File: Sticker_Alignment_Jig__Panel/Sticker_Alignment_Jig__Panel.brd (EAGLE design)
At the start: 200 x 100 mm, 13 parts

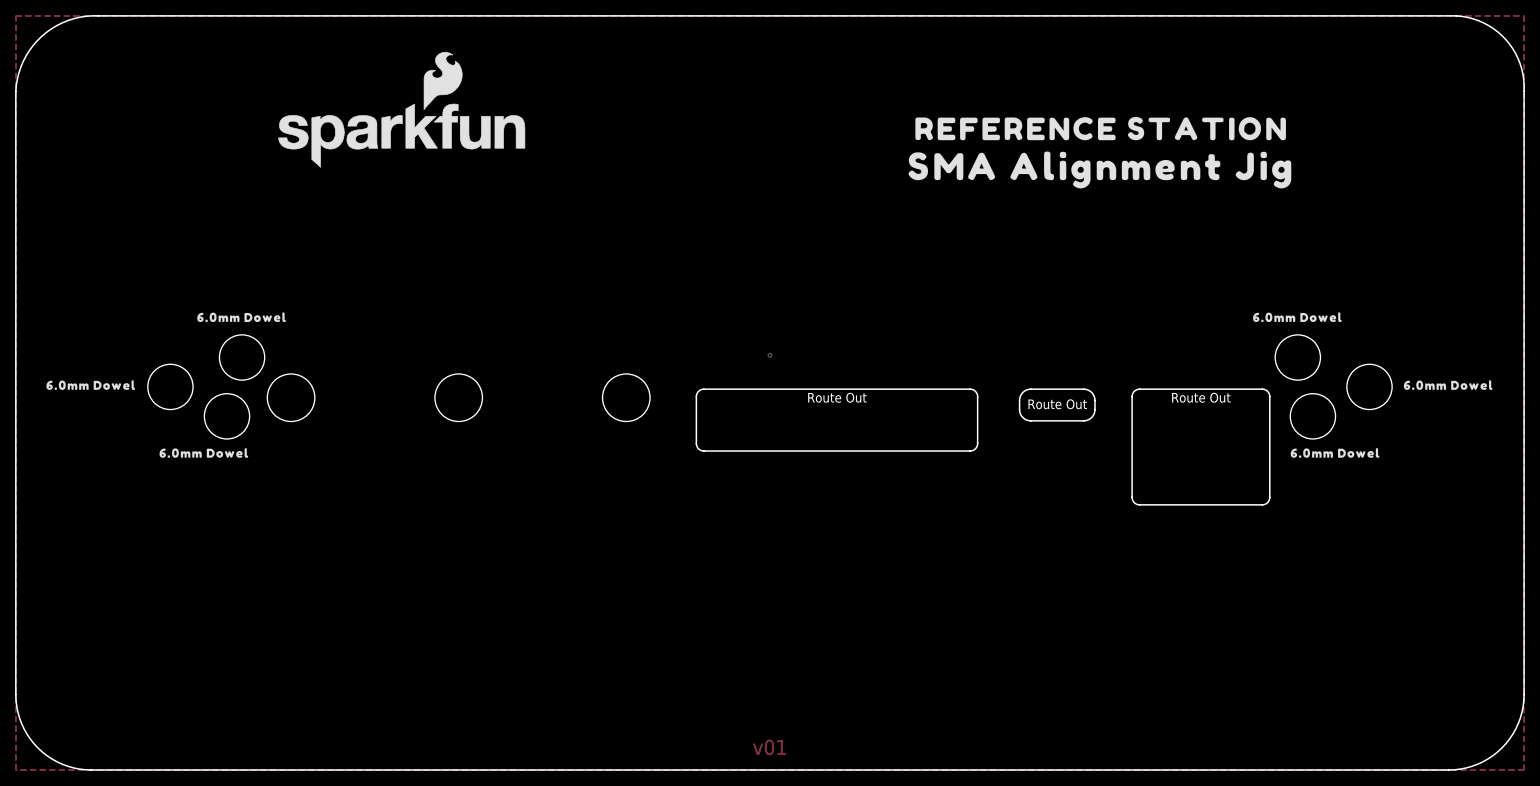
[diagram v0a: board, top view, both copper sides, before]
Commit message: Update sticker alignment jig
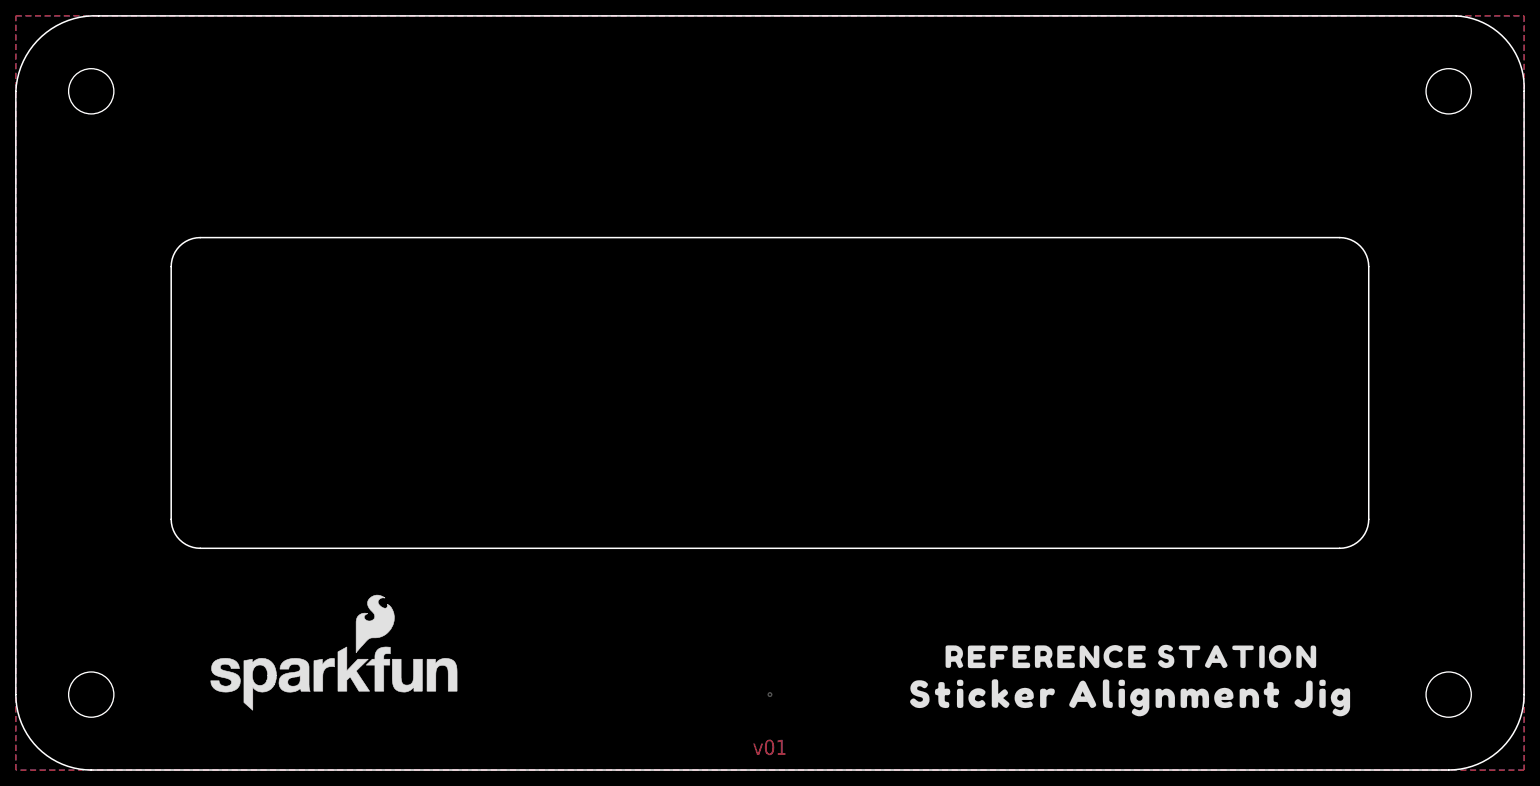
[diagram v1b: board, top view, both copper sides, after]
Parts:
- removed U$10, U$11, U$6, U$7, U$8, U$9: (no value), output:6#0MM_DOWEL0
- removed U$2: 3.5MM_CONNECTOR, CORS_Panels:3.5MM_CONNECTOR
- removed U$3: USB-C, CORS_Panels:USB-C
- removed U$4: ETHERNET, CORS_Panels:ETHERNET
- U$5: device output:SMA_ALIGNMENT_JIG0 -> output:STICKER_ALIGNMENT_JIG0
- moved LOGO1 72.6 mm to (-57.9, -37.9)
- moved U$1 70.1 mm to (48.0, -35.0)
- moved U$5 70.1 mm to (48.0, -40.0)
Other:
- outline, holes or cut-outs redrawn
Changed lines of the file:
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@@
 <drawing>
 <settings>
-<setting alwaysvectorfont="yes"/>
+<setting alwaysvectorfont="no"/>
 <setting verticaltext="up"/>
 </settings>
@@
 <wire x1="-100" y1="40" x2="-100" y2="-40" width="0.2" layer="20"/>
 <text x="0" y="-48" size="2" layer="1" font="vector" ratio="15" align="bottom-center">v01</text>
-<wire x1="76.2" y1="0" x2="-76.2" y2="0" width="0.2" layer="51"/>
-<wire x1="76.2" y1="1.6" x2="-76.2" y2="1.6" width="0.2" layer="51"/>
-<wire x1="-76.2" y1="0" x2="-76.2" y2="1.6" width="0.2" layer="51"/>
-<wire x1="76.2" y1="0" x2="76.2" y2="1.6" width="0.2" layer="51"/>
-<hole x="-79.5" y="0.8" drill="6"/>
-<hole x="79.5" y="0.8" drill="6"/>
-<hole x="-72" y="-3.1" drill="6"/>
-<hole x="-19.05" y="-0.635" drill="6.3"/>
-<hole x="-41.275" y="-0.635" drill="6.3"/>
-<hole x="-63.5" y="-0.635" drill="6.3"/>
-<hole x="-70" y="4.7" drill="6"/>
-<hole x="70" y="4.7" drill="6"/>
-<hole x="72" y="-3.1" drill="6"/>
+<wire x1="-79.4" y1="16.75" x2="-79.4" y2="-16.75" width="0.2" layer="20"/>
+<wire x1="-75.55" y1="-20.6" x2="75.55" y2="-20.6" width="0.2" layer="20"/>
+<wire x1="79.4" y1="-16.75" x2="79.4" y2="16.75" width="0.2" layer="20"/>
+<wire x1="75.55" y1="20.6" x2="-75.55" y2="20.6" width="0.2" layer="20"/>
+<wire x1="-75.55" y1="-20.6" x2="-79.4" y2="-16.75" width="0.2" layer="20" curve="-90"/>
+<hole x="-90" y="40" drill="6"/>
+<hole x="90" y="40" drill="6"/>
+<hole x="90" y="-40" drill="6"/>
+<hole x="-90" y="-40" drill="6"/>
+<wire x1="79.4" y1="-16.75" x2="75.55" y2="-20.6" width="0.2" layer="20" curve="-90"/>
+<wire x1="75.55" y1="20.6" x2="79.4" y2="16.75" width="0.2" layer="20" curve="-90"/>
+<wire x1="-79.4" y1="16.75" x2="-75.55" y2="20.6" width="0.2" layer="20" curve="-90"/>
 </plain>
 <attributes>
@@
 </autorouter>
 <elements>
-<element name="LOGO1" library="SparkFun-Aesthetics" package="SFE_LOGO_NAME_FLAME_.3" value="SFE_LOGO_NAME_FLAME.3_INCH" x="-48.8504" y="34.0889" smashed="yes"/>
-<element name="U$1" library="output" package="REFERENCE_STATION0" value="" x="44" y="35" smashed="yes"/>
+<element name="LOGO1" library="SparkFun-Aesthetics" package="SFE_LOGO_NAME_FLAME_.3" value="SFE_LOGO_NAME_FLAME.3_INCH" x="-57.8504" y="-37.9111" smashed="yes"/>
+<element name="U$1" library="output" package="REFERENCE_STATION0" value="" x="48" y="-35" smashed="yes"/>
 <element name="FRAME1" library="SparkFun-Aesthetics" package="CREATIVE_COMMONS" value="FRAME-LETTER" x="-25" y="-59" smashed="yes">
 <attribute name="DESIGNER" value="" x="-25" y="-59" size="1.778" layer="27" ratio="15" display="off"/>
 <attribute name="REV" value="" x="-25" y="-59" size="1.778" layer="27" ratio="15" display="off"/>
 </element>
-<element name="U$2" library="CORS_Panels" package="3.5MM_CONNECTOR" value="3.5MM_CONNECTOR" x="8.89" y="0" smashed="yes" rot="R180"/>
-<element name="U$3" library="CORS_Panels" package="USB-C" value="USB-C" x="38.1" y="0" smashed="yes" rot="R180"/>
-<element name="U$4" library="CORS_Panels" package="ETHERNET" value="ETHERNET" x="57.15" y="0" smashed="yes" rot="R180"/>
-<element name="U$5" library="output" package="SMA_ALIGNMENT_JIG0" value="" x="44" y="30" smashed="yes"/>
-<element name="U$6" library="output" package="6#0MM_DOWEL0" value="" x="70" y="10" smashed="yes"/>
-<element name="U$7" library="output" package="6#0MM_DOWEL0" value="" x="90" y="1" smashed="yes"/>
-<element name="U$8" library="output" package="6#0MM_DOWEL0" value="" x="75" y="-8" smashed="yes"/>
-<element name="U$9" library="output" package="6#0MM_DOWEL0" value="" x="-75" y="-8" smashed="yes"/>
-<element name="U$10" library="output" package="6#0MM_DOWEL0" value="" x="-90" y="1" smashed="yes"/>
-<element name="U$11" library="output" package="6#0MM_DOWEL0" value="" x="-70" y="10" smashed="yes"/>
+<element name="U$5" library="output" package="STICKER_ALIGNMENT_JIG0" value="" x="48" y="-40" smashed="yes"/>
 </elements>
 <signals>
@@
 <vertex x="-100" y="-50"/>
 </polygon>
-<via x="0" y="5" extent="1-16" drill="0.3"/>
+<via x="0" y="-40" extent="1-16" drill="0.3"/>
 </signal>
 </signals>
